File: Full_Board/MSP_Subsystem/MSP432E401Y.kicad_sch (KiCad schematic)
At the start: 4 parts, among them J1-J3 Conn_01x10, J4-J2 Conn_01x10, J5-J7 Conn_01x10, J8-J6 Conn_01x10

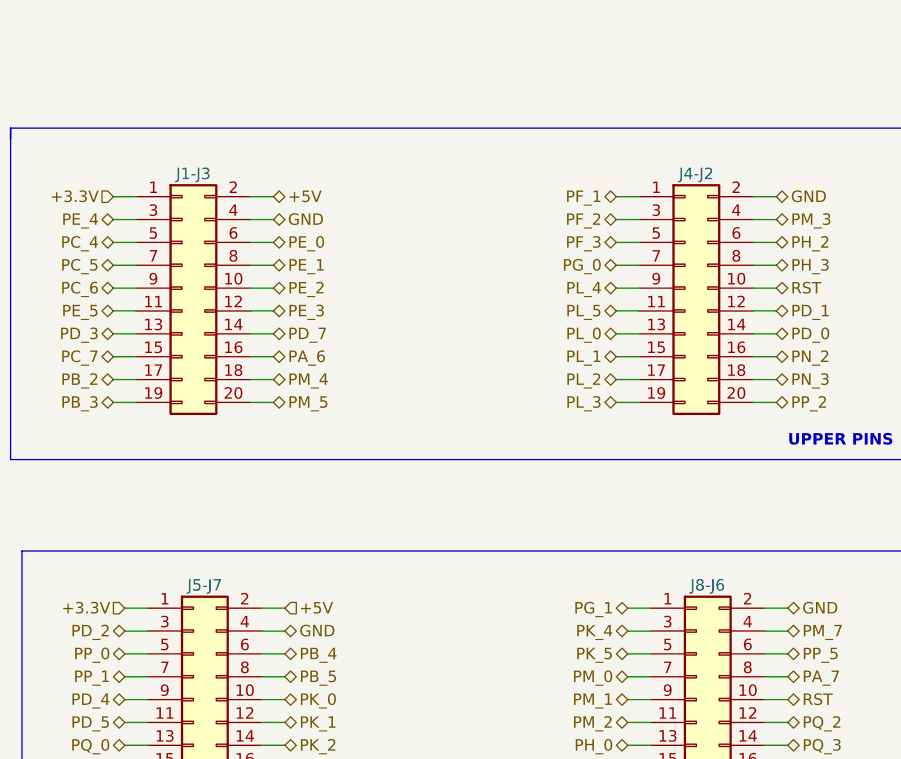
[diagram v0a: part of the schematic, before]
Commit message: Fix annotations, add test points
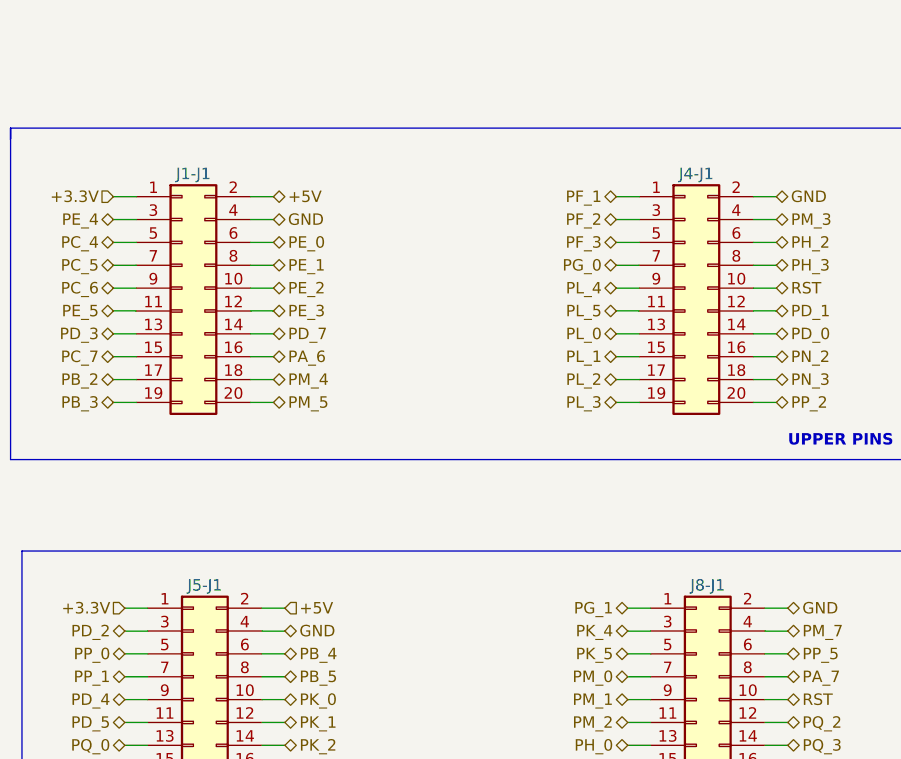
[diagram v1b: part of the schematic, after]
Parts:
- renumbered J1-J3 to J1-J1, J4-J2 to J4-J1, J5-J7 to J5-J1, J8-J6 to J8-J1
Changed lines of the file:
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@@
   (symbol (lib_id "Connector_Generic:Conn_02x10_Odd_Even") (at 167.64 71.12 0) (unit 1)
     (in_bom yes) (on_board yes)
-    (property "Reference" "J4-J2" (id 0) (at 168.91 58.42 0))
+    (property "Reference" "J4-J1" (id 0) (at 168.91 58.42 0))
     (property "Value" "Conn_01x10" (id 1) (at 165.1 87.63 0)
       (effects (font (size 1.27 1.27)) hide)
@@
   (symbol (lib_id "Connector_Generic:Conn_02x10_Odd_Even") (at 113.03 116.84 0) (unit 1)
     (in_bom yes) (on_board yes)
-    (property "Reference" "J5-J7" (id 0) (at 114.3 104.14 0))
+    (property "Reference" "J5-J1" (id 0) (at 114.3 104.14 0))
     (property "Value" "Conn_01x10" (id 1) (at 115.57 120.65 0)
       (effects (font (size 1.27 1.27)) (justify left) hide)
@@
   (symbol (lib_id "Connector_Generic:Conn_02x10_Odd_Even") (at 168.91 116.84 0) (unit 1)
     (in_bom yes) (on_board yes)
-    (property "Reference" "J8-J6" (id 0) (at 170.18 104.14 0))
+    (property "Reference" "J8-J1" (id 0) (at 170.18 104.14 0))
     (property "Value" "Conn_01x10" (id 1) (at 166.37 133.35 0)
       (effects (font (size 1.27 1.27)) hide)
@@
   (symbol (lib_id "Connector_Generic:Conn_02x10_Odd_Even") (at 111.76 71.12 0) (unit 1)
     (in_bom yes) (on_board yes)
-    (property "Reference" "J1-J3" (id 0) (at 113.03 58.42 0))
+    (property "Reference" "J1-J1" (id 0) (at 113.03 58.42 0))
     (property "Value" "Conn_01x10" (id 1) (at 114.3 74.93 0)
       (effects (font (size 1.27 1.27)) (justify left) hide)

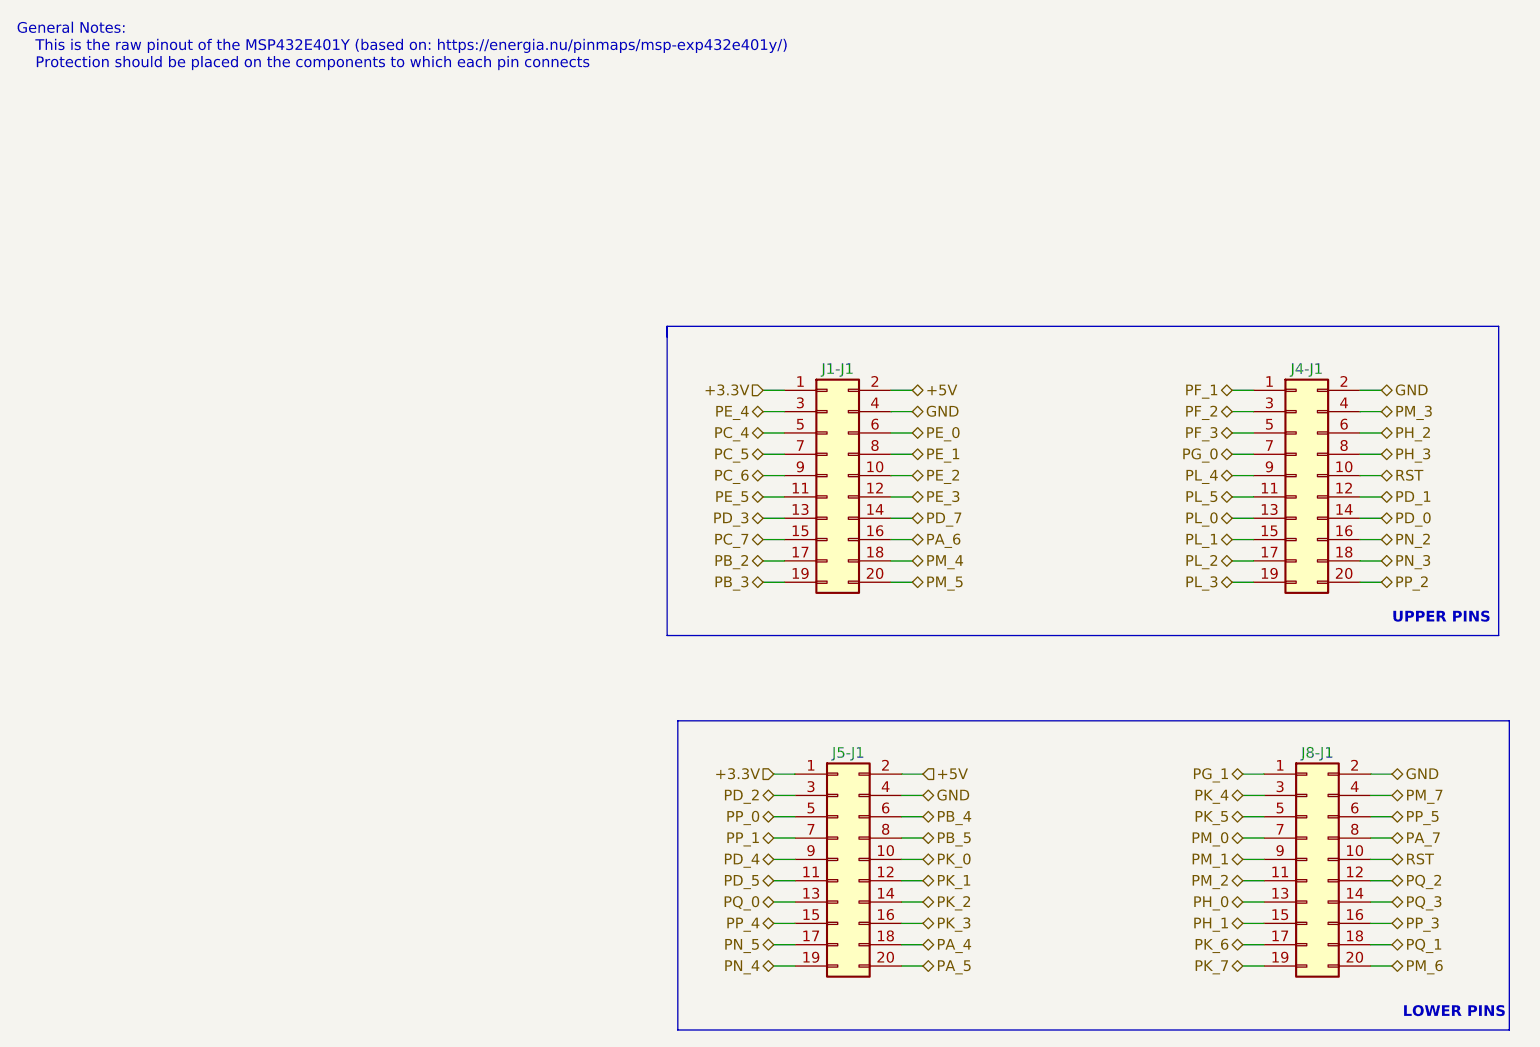
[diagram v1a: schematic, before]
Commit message: Add screenshots of each subsystem
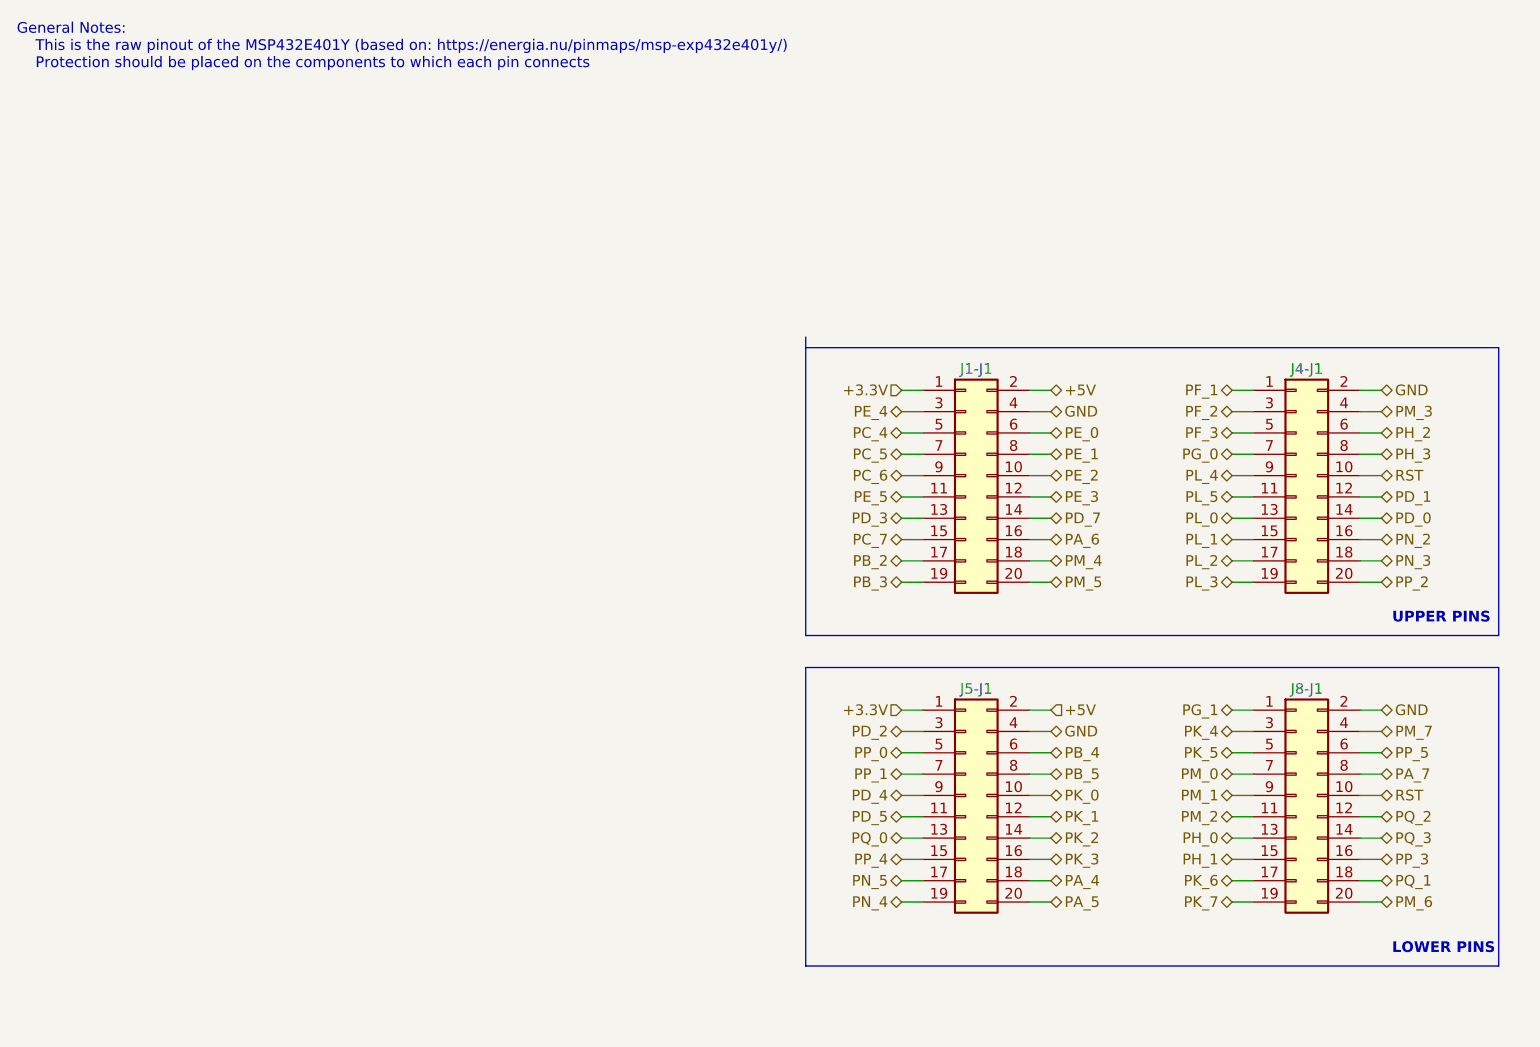
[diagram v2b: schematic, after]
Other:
- moved on the sheet: J1-J1, J5-J1, J8-J1

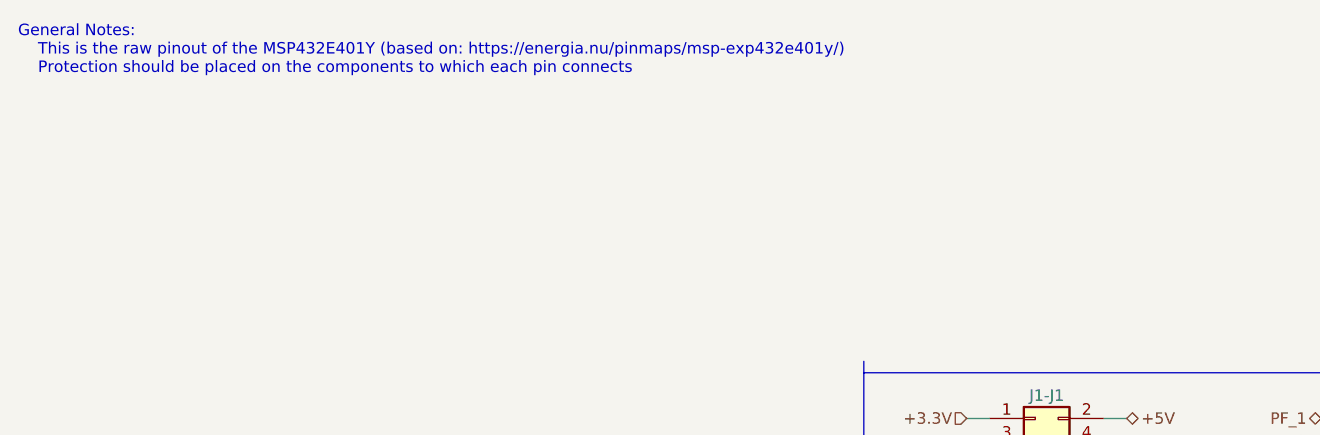
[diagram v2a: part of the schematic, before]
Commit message: Redo sensor network, redo MSP432 connections, redo LED subsystem, add shunts throughout, ERC still passes
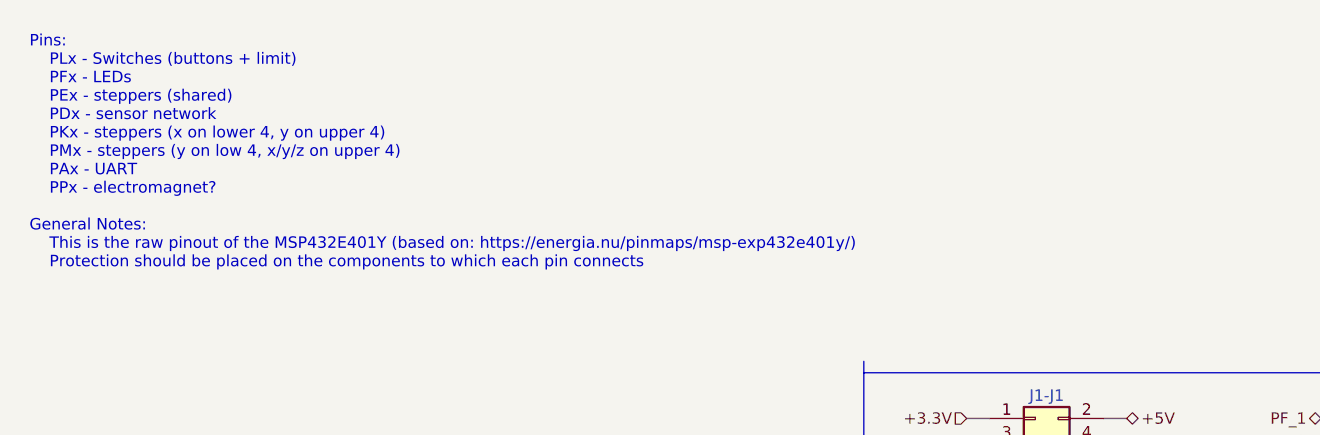
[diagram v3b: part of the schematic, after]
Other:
- note added: "Pins: PLx - Switches (buttons + limit) PFx - LEDs PEx - steppers (shared) PDx - sensor network PKx - steppers (x on lower 4, y on upper 4) PMx - steppers (y on low 4, x/y/z on upper 4) PAx - UART PPx - electromagnet? General Notes: This is the raw pinout of the MSP432E401Y (based on: https://energia.nu/pinmaps/msp-exp432e401y/) Protection should be placed on the components to which each pin conne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"
- note removed: "General Notes: This is the raw pinout of the MSP432E401Y (based on: https://energia.nu/pinmaps/msp-exp432e401y/) Protection should be placed on the components to which each pin connects"
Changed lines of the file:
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@@
     (stroke (width 0) (type default) (color 0 0 0 0))
   )
-  (text "General Notes:\n	This is the raw pinout of the MSP432E401Y (based on: https://energia.nu/pinmaps/msp-exp432e401y/)\n	Protection should be placed on the components to which each pin connects"
-    (at 15.24 22.86 0)
+  (text "Pins:\n	PLx - Switches (buttons + limit)\n	PFx - LEDs\n	PEx - steppers (shared)\n	PDx - sensor network\n	PKx - steppers (x on lower 4, y on upper 4)\n	PMx - steppers (y on low 4, x/y/z on upper 4)\n	PAx - UART\n	PPx - electromagnet?\n\nGeneral Notes:\n	This is the raw pinout of the MSP432E401Y (based on: https://energia.nu/pinmaps/msp-exp432e401y/)\n	Protection should be placed on the components to which each pin connects"
+    (at 16.51 44.45 0)
     (effects (font (size 1.27 1.27)) (justify left bottom))
   )
